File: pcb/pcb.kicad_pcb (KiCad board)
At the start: 2 copper layers, 21 x 51.1 mm, 38 parts, among them J1 USB_C_Receptacle_USB2.0_14P, J2 Conn_01x20, J3 Conn_01x20, J4 Conn_01x03, SW1 SW_Push, U1 RP2040, U2 MCP1700x-330xxTT, U3 W25Q16JVZPIQ, Y1 12 MHz

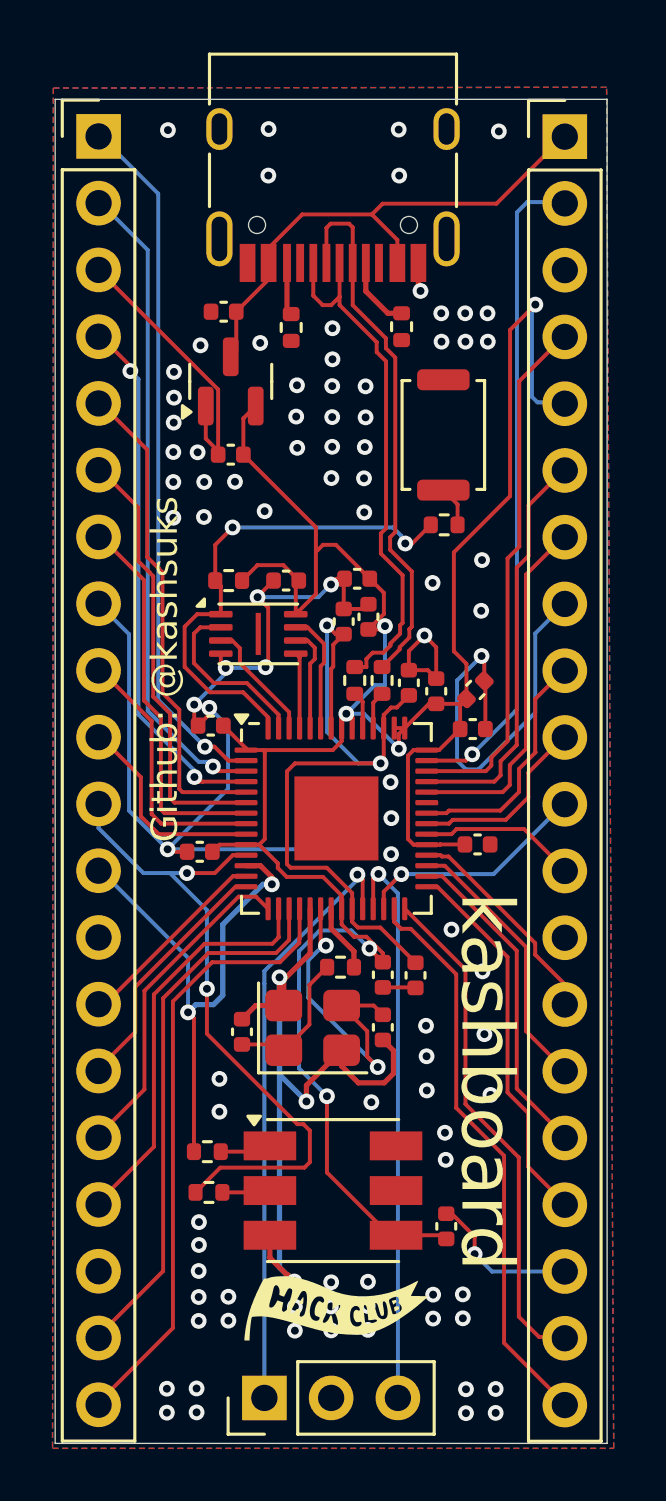
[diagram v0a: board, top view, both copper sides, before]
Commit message: replaced the apa102 with sk6182 neopixel
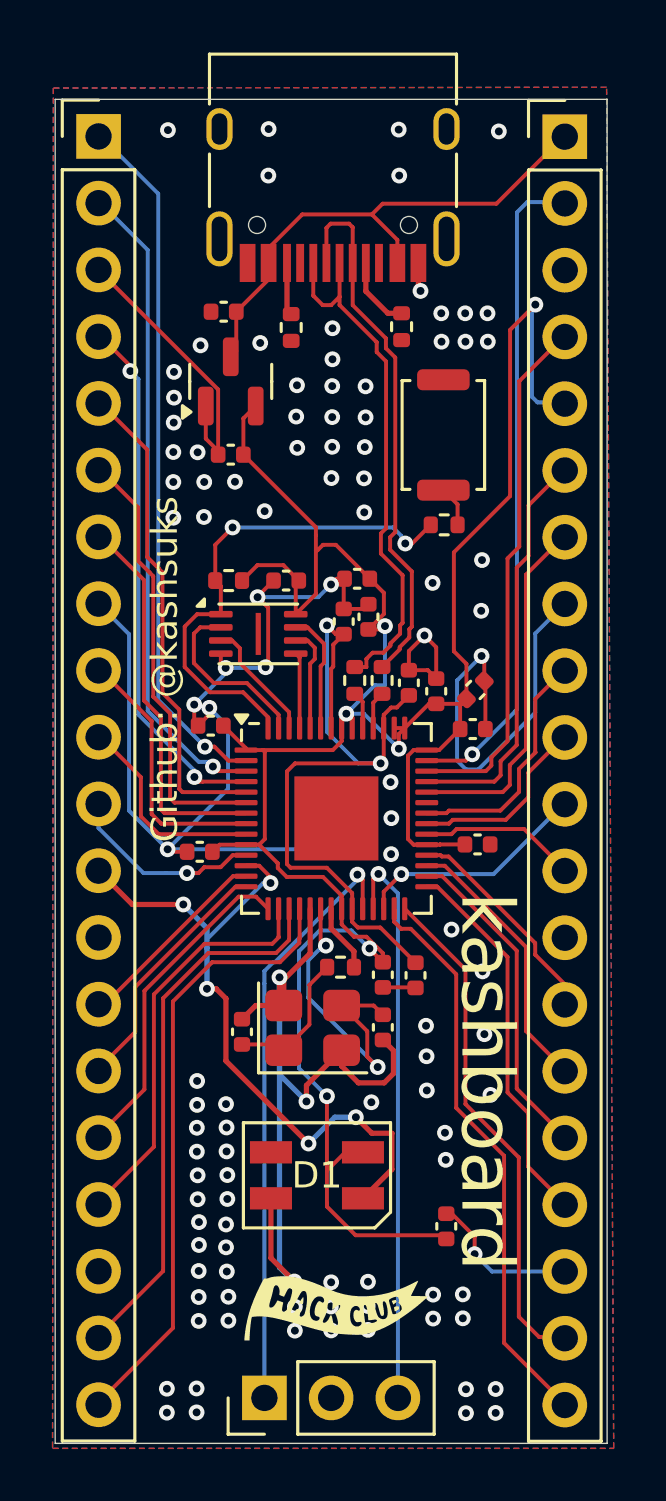
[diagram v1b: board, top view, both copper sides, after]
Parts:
- removed D2: APA102, LED_SMD:LED_RGB_5050-6
- removed R8, R9: 100, Resistor_SMD:R_0402_1005Metric
- added D1: SK6812MINI, LED_SMD:LED_SK6812MINI_PLCC4_3.5x3.5mm_P1.75mm, F.Cu at (100.8, 105.7)
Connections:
- net GPIO9 renamed NEOPIXEL
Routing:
- net GPIO8: track 26.6 -> 8.25 mm, vias 2 -> 1
- net NEOPIXEL: track 20.5 -> 26.8 mm, vias 2 -> 5
- net +3V3: track 99.7 -> 102.1 mm
- net Net-(D2-DI): track 1.96 -> 0.00 mm
- net Net-(D2-CI): track 1.84 -> 0.00 mm
- net GND: track 112.8 -> 114.3 mm, vias 98 -> 110
